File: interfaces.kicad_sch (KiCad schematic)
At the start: 33 parts, among them J3 SI-51005-F

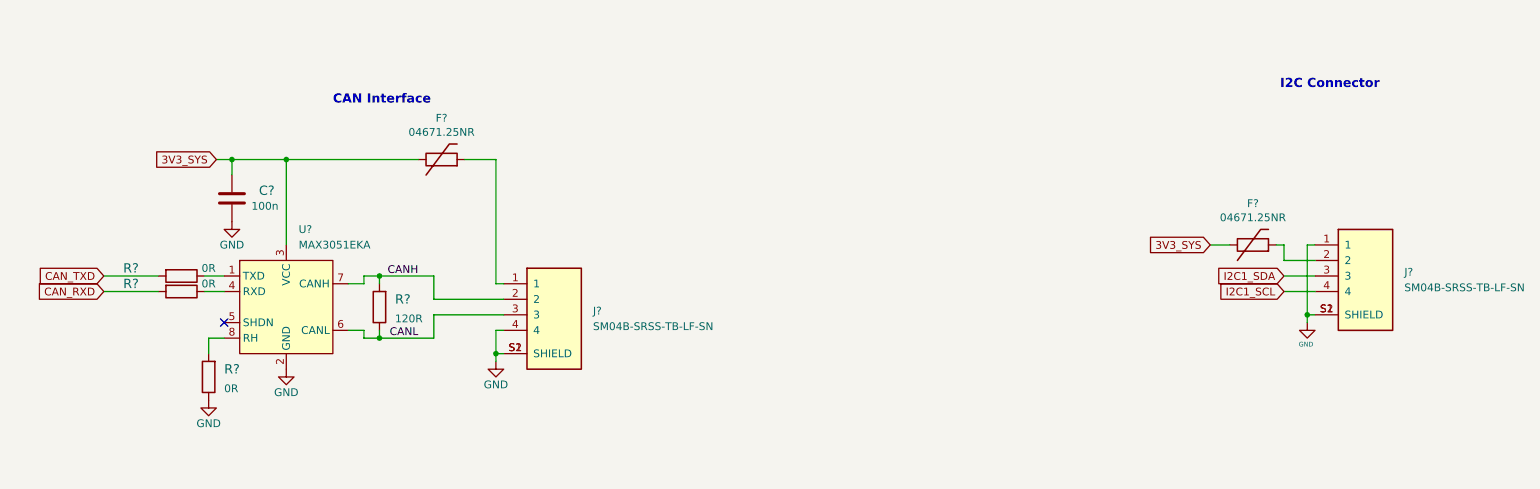
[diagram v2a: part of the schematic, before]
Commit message: Resolve TOOD on USB sheet
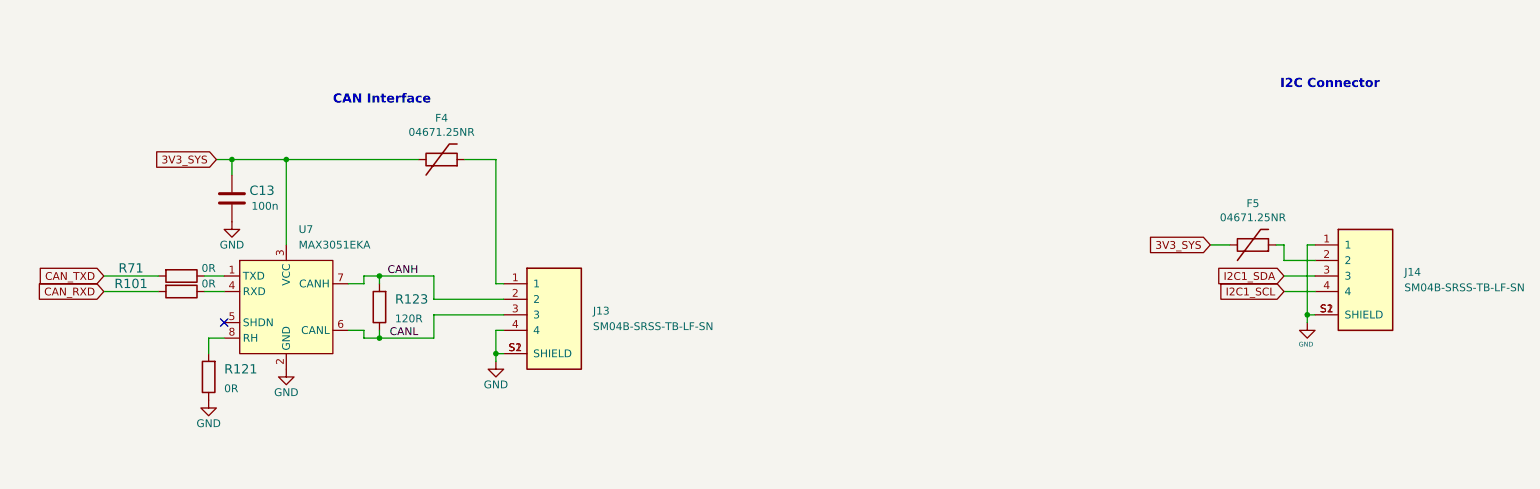
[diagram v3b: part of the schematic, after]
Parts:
- gave numbers to parts that had none: 10
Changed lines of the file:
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@@
   (symbol (lib_id "jetson-nano-baseboard:SM04B-SRSS-TB-LF-SN") (at 311.785 71.12 0) (unit 1)
     (in_bom yes) (on_board yes) (fields_autoplaced)
-    (property "Reference" "J?" (id 0) (at 321.31 69.2149 0)
+    (property "Reference" "J14" (id 0) (at 321.31 69.2149 0)
       (effects (font (size 1.27 1.27)) (justify left))
     )
@@
   (symbol (lib_id "jetson-nano-baseboard:SM04B-SRSS-TB-LF-SN") (at 179.07 77.47 0) (unit 1)
     (in_bom yes) (on_board yes) (fields_autoplaced)
-    (property "Reference" "J?" (id 0) (at 188.595 75.5649 0)
+    (property "Reference" "J13" (id 0) (at 188.595 75.5649 0)
       (effects (font (size 1.27 1.27)) (justify left))
     )
@@
   (symbol (lib_id "jetson-nano-baseboard:GND") (at 138.43 85.09 0) (unit 1)
     (in_bom yes) (on_board yes)
-    (property "Reference" "#PWR?" (id 0) (at 138.43 91.44 0)
+    (property "Reference" "#PWR0103" (id 0) (at 138.43 91.44 0)
       (effects (font (size 1.27 1.27)) hide)
     )
@@
   (symbol (lib_id "jetson-nano-baseboard:GND") (at 125.73 90.17 0) (unit 1)
     (in_bom yes) (on_board yes)
-    (property "Reference" "#PWR?" (id 0) (at 125.73 96.52 0)
+    (property "Reference" "#PWR0104" (id 0) (at 125.73 96.52 0)
       (effects (font (size 1.27 1.27)) hide)
     )
@@
   (symbol (lib_id "jetson-nano-baseboard:R_120R_0402") (at 153.67 74.93 90) (unit 1)
     (in_bom yes) (on_board yes) (fields_autoplaced)
-    (property "Reference" "R?" (id 0) (at 156.21 73.66 90)
+    (property "Reference" "R123" (id 0) (at 156.21 73.66 90)
       (effects (font (size 1.524 1.524)) (justify right))
     )
@@
   (symbol (lib_id "jetson-nano-baseboard:R_0R_0402") (at 121.285 69.85 180) (unit 1)
     (in_bom yes) (on_board yes)
-    (property "Reference" "R?" (id 0) (at 113.03 68.58 0)
+    (property "Reference" "R71" (id 0) (at 113.03 68.58 0)
       (effects (font (size 1.524 1.524)))
     )
@@
   (symbol (lib_id "jetson-nano-baseboard:R_0R_0402") (at 125.73 86.36 90) (unit 1)
     (in_bom yes) (on_board yes) (fields_autoplaced)
-    (property "Reference" "R?" (id 0) (at 128.27 85.09 90)
+    (property "Reference" "R121" (id 0) (at 128.27 85.09 90)
       (effects (font (size 1.524 1.524)) (justify right))
     )
@@
   (symbol (lib_id "jetson-nano-baseboard:04671.25NR") (at 163.83 50.8 0) (unit 1)
     (in_bom yes) (on_board yes)
-    (property "Reference" "F?" (id 0) (at 163.83 44.0182 0))
+    (property "Reference" "F4" (id 0) (at 163.83 44.0182 0))
     (property "Value" "04671.25NR" (id 1) (at 163.83 46.3296 0))
     (property "Footprint" "jetson-nano-baseboard-footprints:0603-Fuse-Littelfuse-0467" (id 2) (at 165.1 56.515 0)
@@
   (symbol (lib_id "jetson-nano-baseboard:GND") (at 172.72 83.82 0) (unit 1)
     (in_bom yes) (on_board yes)
-    (property "Reference" "#PWR?" (id 0) (at 172.72 90.17 0)
+    (property "Reference" "#PWR0102" (id 0) (at 172.72 90.17 0)
       (effects (font (size 1.27 1.27)) hide)
     )
@@
   (symbol (lib_id "jetson-nano-baseboard:MAX3051EKA") (at 138.43 69.85 0) (unit 1)
     (in_bom yes) (on_board yes) (fields_autoplaced)
-    (property "Reference" "U?" (id 0) (at 140.4494 62.23 0)
+    (property "Reference" "U7" (id 0) (at 140.4494 62.23 0)
       (effects (font (size 1.27 1.27)) (justify left))
     )
@@
   (symbol (lib_id "jetson-nano-baseboard:GND") (at 305.435 77.47 0) (unit 1)
     (in_bom yes) (on_board yes)
-    (property "Reference" "#GND_?" (id 0) (at 305.435 77.47 0)
+    (property "Reference" "#GND_0169" (id 0) (at 305.435 77.47 0)
       (effects (font (size 0.508 0.508)) hide)
     )
@@
   (symbol (lib_id "jetson-nano-baseboard:04671.25NR") (at 296.545 64.77 0) (unit 1)
     (in_bom yes) (on_board yes)
-    (property "Reference" "F?" (id 0) (at 296.545 57.9882 0))
+    (property "Reference" "F5" (id 0) (at 296.545 57.9882 0))
     (property "Value" "04671.25NR" (id 1) (at 296.545 60.2996 0))
     (property "Footprint" "jetson-nano-baseboard-footprints:0603-Fuse-Littelfuse-0467" (id 2) (at 297.815 70.485 0)
@@
   (symbol (lib_id "jetson-nano-baseboard:R_0R_0402") (at 121.285 72.39 180) (unit 1)
     (in_bom yes) (on_board yes)
-    (property "Reference" "R?" (id 0) (at 113.03 71.12 0)
+    (property "Reference" "R101" (id 0) (at 113.03 71.12 0)
       (effects (font (size 1.524 1.524)))
     )
@@
   (symbol (lib_id "jetson-nano-baseboard:C_100n_0402") (at 129.54 57.15 180) (unit 1)
     (in_bom yes) (on_board yes)
-    (property "Reference" "C?" (id 0) (at 136.525 55.88 0)
+    (property "Reference" "C13" (id 0) (at 136.525 55.88 0)
       (effects (font (size 1.524 1.524)) (justify left))
     )
@@
   (symbol (lib_id "jetson-nano-baseboard:GND") (at 129.54 60.96 0) (unit 1)
     (in_bom yes) (on_board yes)
-    (property "Reference" "#PWR?" (id 0) (at 129.54 67.31 0)
-      (effects (font (size 1.27 1.27)) hide)
-    )
+    (property "Reference" "#PWR0101" (id 0) (at 129.54 67.31 0)
+      (effects (font (size 1.27 1.27)) hide)
+    )

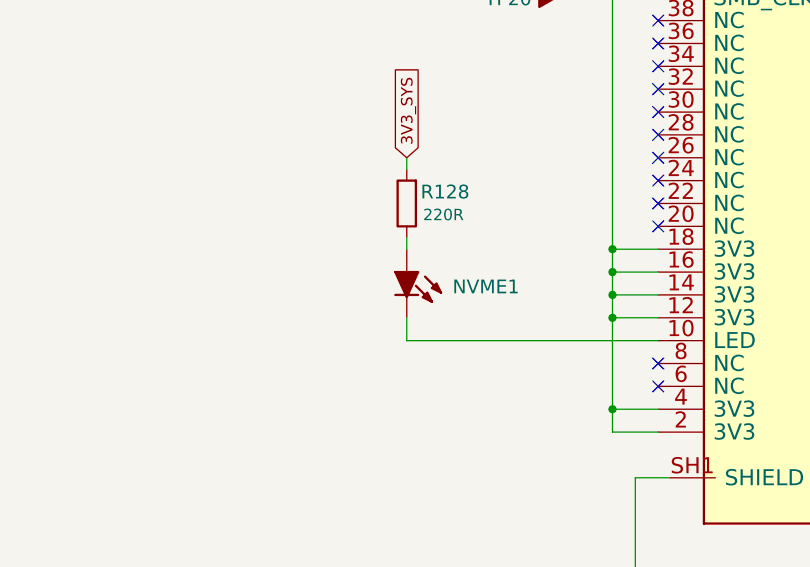
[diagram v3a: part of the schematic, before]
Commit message: Continue placement, mix USB SS signals as HD3SS3220 allows for it
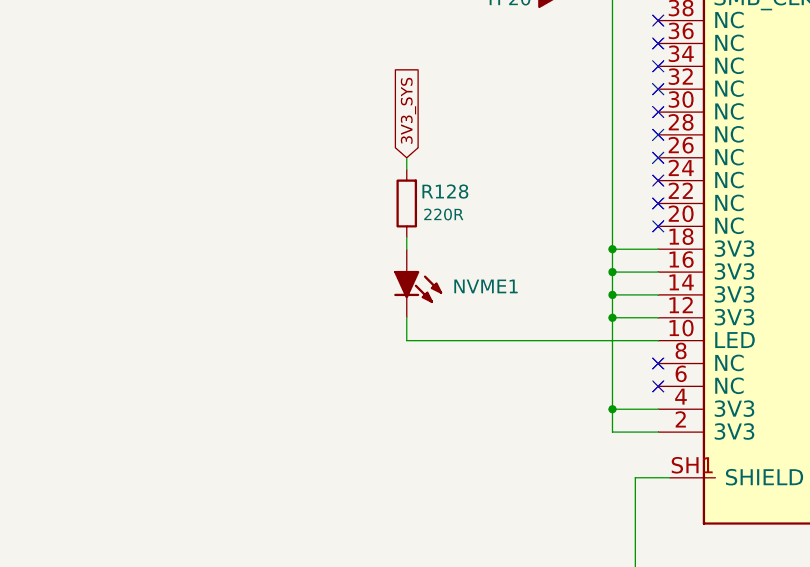
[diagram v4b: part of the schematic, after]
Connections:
- net at R128.1: now also NVME1.1 (A); no longer NVME1.A
- net at J8.10 (LED): now also NVME1.2 (K); no longer NVME1.K
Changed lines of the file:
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@@
       (effects (font (size 1.27 1.27)) hide)
     )
-    (pin "A")
-    (pin "K")
+    (pin "1")
+    (pin "2")
   )
   (symbol (lib_id "jetson-nano-baseboard:9774040151") (at 139.7 236.22 180) (unit 1)
